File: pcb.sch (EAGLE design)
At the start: 57 parts, among them U2 ISO7221A_D_8, U3 MAX232E_D_16, U4 ISO7221A_D_8, U5 DCH010505S_EDJ_4, U6 REG101-3_DBV_5, U7 DCH010505S_EDJ_4, U8 MSP430G2553_PW_28

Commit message: Updated UART and expansion plug
Moved to true dual UART (one timer based)
Added remaining unused pins to expansion plug
finished first draft routing...no DRC check
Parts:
- removed U$4, U$5: TS5A3159-Q1, TI:TS5A3159-Q1
- JP10: device jumper:JP6Q -> jumper:JP8Q
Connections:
- removed net RX: U$4.COM, U8.P1.1/TA0.0/UCA0RXD/UCA0SOMI/A1/CA1
- removed net TX: U$5.COM, U8.P1.2/TA0.1/UCA0TXD/PUCA0SIMO/A2/CA2
- removed net UART_MODE: U$4.IN, U$5.IN, U8.P3.5/TA0.1
- new net GPIO1: JP10.11, U8.P3.7/TA1CLK/CAOUT
- new net GPIO2: JP10.13, U8.P3.6/TA0.2
- new net GPIO3: JP10.16, U8.P3.4/TA0.0
- net ENCODER_A_MCU: now also U8.P2.0/TA1.0; no longer U8.P1.5/TA0.0/UCB0CLK/UCA0STE/A5/CA5/TMS
- net ENCODER_B_MCU: now also C25.2, R8.2; no longer C26.1, R9.2
- net ENCODER_PUSH: now also C26.1, R9.2; no longer C25.2, R8.2
- net GND: now also JP10.3; no longer JP10.2, U$4.GND, U$5.GND
- net LASER_ON: now also JP10.14; no longer JP10.5
- net N$18: now also JP10.7; no longer JP10.9
- net N$19: now also JP10.5; no longer JP10.7
- net RST: now also JP10.15
- net RX1: now also U8.P1.1/TA0.0/UCA0RXD/UCA0SOMI/A1/CA1; no longer U$4.NC
- net RX2: now also U8.P1.5/TA0.0/UCB0CLK/UCA0STE/A5/CA5/TMS; no longer U$4.NO
- net SCL: now also JP10.9; no longer JP10.11
- net TX1: now also U8.P1.2/TA0.1/UCA0TXD/PUCA0SIMO/A2/CA2; no longer U$5.NC
- net TX2: now also U8.P3.5/TA0.1; no longer U$5.NO
- net VCC_3V: no longer U$4.VCC, U$5.VCC
- net VCC_5V: now also JP10.2; no longer JP10.3
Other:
- moved on the sheet: C1, C10, C11, C12, C13, C14, C15, C16, C17, C18, C19, C20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

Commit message: updated layout and board
Fixed interlock design
Added analog front end to analog inputs
changed MCU to MSP450 5 series
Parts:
- removed C22, C23, C24, C25, C26, C27: (no value), adafruit:C-USC1206
- removed JP10: (no value), jumper:JP8Q
- removed QF1: 10G7A-12.5KHZ, crystal:10G7A-12.5KHZ
- removed R12: (no value), adafruit:R-US_M1206
- removed U$3: TS5A3159-Q1, TI:TS5A3159-Q1
- added C2, C29: 2.2 uF, adafruit:C-USC1206
- added C30: 4.7 uF, adafruit:C-USC1206
- added C31, C32, C33, C34: 0.1 uF, adafruit:C-USC1206
- added JP2: (no value), adafruit:PINHD-2X4
- added JP3, JP6: (no value), jumper:JP2E
- added Q2: (no value), adafruit:XTAL-4-3225
- added R14: 500k, adafruit:R-US_M1206
- added R15: 10k, adafruit:R-US_M1206
- added R4: (no value), adafruit:R-US_M1206
- added SV1: (no value), con-lsta:FE08-2
- added SV3: (no value), con-lsta:FE06-2
- added U$4: 10k, adafruit:TRIMPOTTC33X
- added U$5: 100 nF, TI:468M-801-XXX
- added U$6: 3 uH, adafruit:FB
- added U1: MSP430F5172_DA_38, TI:MSP430F5172_DA_38
- added U10: DCH010505S_EDJ_4, TI:DCH010505S_EDJ_4
- added U11: ISO7221A_D_8, TI:ISO7221A_D_8
- added U12, U13: TS5A3357_DCU_8, TI:TS5A3357_DCU_8
- added U14: TLV2242_D_8, TI:TLV2242_D_8
- C1, C6, C7, C8: value (none) -> 1 uF
- C10, C11, C12, C18, C19, C3, C4: value (none) -> 0.1 uF
- C13, C16: value (none) -> 2.2 uF
- C14, C17: value (none) -> 4.7 uF
- C15, C5: value (none) -> 10 uF
- C20: value (none) -> 0.01 uF
- C9: value (none) -> 2.2 nF
- JP4: device jumper:JP4E -> con-lsta:FE07-2
- JP7: device con-subd:F09HP -> jumper:JP2E
- R1: value (none) -> 1M; device adafruit:R-US_M1206 -> adafruit:R-US_R1206
- R10: value (none) -> 47k
- R11: value (none) -> 750k
- R2, R3: value (none) -> 43k
- R5: value (none) -> 500k
- R6: value (none) -> 0R; device adafruit:R-US_M1206 -> adafruit:R-US_R1206
- R7: value (none) -> 100k; device adafruit:R-US_M1206 -> resistor-bourns:2QSP16-8
- R8: value (none) -> 600k; device adafruit:R-US_M1206 -> adafruit:R-US_R1206
- R9: value (none) -> 400k; device adafruit:R-US_M1206 -> adafruit:R-US_R1206
- U$1, U$2: value FB -> 3 uH
- U8: value MSP430G2553_PW_28 -> TCA6416A_PW_24; device TI:MSP430G2553_PW_28 -> TI:TCA6416A_PW_24
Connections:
- net N$20 renamed SERIAL_VCC
- removed net ENCODER_A_MCU: C27.1, R10.2, U8.P2.0/TA1.0
- removed net ENCODER_B_MCU: C25.2, R8.2, U8.P3.0/TA0.2
- removed net ENCODER_PUSH: C26.1, R9.2, U8.P3.1/TA1.0
- removed net GPIO1: JP10.11, U8.P3.7/TA1CLK/CAOUT
- removed net GPIO2: JP10.13, U8.P3.6/TA0.2
- removed net GPIO3: JP10.16, U8.P3.4/TA0.0
- removed net LASER_ENABLE: U8.P2.3/TA1.0, X2.1
- removed net LASER_ILK_LED: R11.2, U8.P2.2/TA1.1
- removed net LASER_ON: JP10.14, U8.P3.3/TA1.2
- removed net LASER_ON_LED: R12.2, U8.P3.2/TA1.1
- removed net MCU_TTL: U$3.NC, U2.INA, U8.P2.5/TA1.2
- removed net N$16: C22.1, QF1.3, R7.2
- removed net N$19: JP10.5, R12.1
- removed net TTL_CTL: U$3.IN, U8.P2.4/TA1.2
- new net 3VIO-0: R7.15, U1.PJ.0/SMCLK/TDO/CB6
- new net 3VIO-0H: R7.8, SV3.1, U$5.1
- new net 3VIO-1: R7.14, U1.PJ.1/MCLK/TDI/TCLK/CB7
- new net 3VIO-1H: R7.7, SV3.2, U$5.2
- new net 3VIO-2: R7.13, U1.PJ.2/ADC10CLK/TMS/CB8
- new net 3VIO-2H: R7.6, SV3.4, U$5.3
- new net 3VIO-3: R7.12, U1.PJ.3/ACLK/TCK/CB9
- new net 3VIO-3H: R7.5, SV3.6, U$5.4
- new net 3VIO-4: R7.11, U1.P3.3/PM_TA0CLK/PM_CBOUT/CB13
- new net 3VIO-4H: R7.4, SV3.8, U$5.5
- new net 3VIO-5: R7.10, U1.P3.2/PM_TD0.0/PM_SMCLK/CB14
- new net 3VIO-5H: R7.3, SV3.10, U$5.6
- new net 3VIO-6: R7.9, U1.PJ.6/TD1CLK/TD0.1/CB15
- new net 3VIO-6H: R7.2, SV3.12, U$5.7
- new net 5VIO-0: JP2.7, U1.P1.6/PM_TD0.0
- new net 5VIO-1: JP2.5, U1.P2.0/PM_TD0.2
- new net 5VIO-2: JP2.3, U1.P2.1/PM___TD1.0
- new net 5VIO-3: JP2.1, U1.P2.2/PM_TD1.1
- new net CONTRAST: SV1.3, U$4.S
- new net DB0: SV1.7, U8.P00
- new net DB1: SV1.8, U8.P01
- new net DB2: SV1.9, U8.P02
- new net DB3: SV1.10, U8.P03
- new net DB4: SV1.11, U8.P04
- new net DB5: SV1.12, U8.P05
- new net DB6: SV1.13, U8.P06
- new net DB7: SV1.14, U8.P07
- new net ENABLE: SV1.6, U8.P11
- new net EXT_SRC-A: U1.P2.5/PM_TEC0FLT0/PM_TD0.1, U13.IN1
- new net EXT_SRC-B: U1.P2.4/PM_TEC0CLR/PM_TEC0FLT2_/PM_TD0.0, U13.IN2
- new net EXT_TTL: JP2.2, U12.NO1, U13.NO1
- new net ITL_POWER: C29.1, U$6.2, U10.VI+
- new net LASER_CURRENT_3V: U1.P1.0/PM_UCA0CLK/PM_UCB0STE/A0*/CB0, U14.1IN-, U14.1OUT
- new net LASER_ILK_HIGH: R11.1, U11.OUTA
- new net LASER_SRC-A: U1.P2.7/PM_TEC1CLR/PM_TEC1FLT1/PM_TD1.0, U12.IN1
- new net LASER_SRC-B: U1.P2.6/PM_TEC0FLT1/PM_TD0.2, U12.IN2
- new net LASER_TEMPERATURE_3V: U1.P1.3/PM_UCB0CLK/PM_UCA0STE/A3*/CB3, U14.2IN-, U14.2OUT
- new net MCU_TTL1: U1.P3.1/PM_TEC1FLT0/PM_TD1.2, U12.NO0, U13.NO2
- new net MCU_TTL2: U1.P3.0/PM_TEC1FLT2/PM_TD1.1, U13.NO0
- new net N$21: Q2.X1, U1.PJ.4/XOUT
- new net N$22: Q2.X2, U1.PJ.5/XIN
- new net N$24: C34.1, U1.VCORE
- new net N$27: C2.1, R14.2, U10.VO+, U11.VCC2
- new net N$28: C2.2, JP3.3, U10.VO-, U11.GND2
- new net N$35: JP3.1, R14.1
- new net R/W: SV1.5, U8.P12
- new net RS: SV1.4, U8.P10
- new net TTL_OUT: U13.COM, U2.INA
- new net VCC_LED: R4.1, SV1.15
- net GND: now also C29.2, C30.2, C31.2, C32.2, C33.2, C34.2, JP2.6, JP4.9, Q2.G1, R1.1, R8.1, SV1.1, SV1.16, SV3.5, U$4.A, U$5.BUS, U$5.BUS2, U1.AVSS, U1.DVSS, U1.DVSS_2, U10.VI-, U11.GND1, U12.GND, U13.GND, U14.GND, U8.GND; no longer C22.2, C23.2, C24.2, C25.1, C26.2, C27.2, JP10.3, JP4.3, QF1.2, U$3.GND, U8.DVSS
- net LASER_CURRENT: now also R9.2; no longer U8.P1.0/TA0CLK/ACLK/A0/CA0
- net LASER_ILK: now also R11.2, U1.P2.3/PM_TD1.2, X2.1; no longer JP10.4, R1.1, U8.P2.1/TA1.1
- net LASER_TEMPERATURE: now also R6.2; no longer U8.P1.3/ADC10CLK/CAOUT/VREF-/VEREF-/A3/CA3
- net LASER_TTL: now also U12.COM; no longer U$3.COM
- net N$10: now also R8.2, R9.1, U14.1IN+; no longer JP10.8, R8.1
- net N$12: now also R5.2, U11.INA; no longer R5.1, U8.XIN/P2.6/TA0.1
- net N$14: now also JP3.2, R5.1; no longer R7.1, U8.XOUT/P2.7
- net N$15: now also R15.1, U8.*RESET; no longer C9.1, QF1.1, R5.2
- net N$17: now also JP4.2, JP7.3; no longer JP10.10, R10.1
- net N$18: now also JP4.4, JP7.1; no longer JP10.7, R11.1
- net N$8: now also R1.2, R6.1, U14.2IN+; no longer JP10.6, R9.1
- net RS232_RX: now also JP6.3; no longer JP7.2
- net RS232_TX: now also JP6.2; no longer JP7.3
- net RST: now also C9.1, JP4.1, R10.1, U1.*RST/NMI/SBWTDIO; no longer C24.1, JP10.15, JP4.2, R6.1, U8.*RST/NMI/SBWTDIO
- net RX1: now also U1.P1.2/PM_UCA0RXD/PM_UCA0SOMI/A2*/CB2; no longer U8.P1.1/TA0.0/UCA0RXD/UCA0SOMI/A1/CA1
- net RX2: now also U1.P3.6/PM_TA0.1/A7*/VEREF-*_/CB11; no longer U8.P1.5/TA0.0/UCB0CLK/UCA0STE/A5/CA5/TMS
- net SCL: now also SV3.7, U1.P1.5/PM_UCB0SOMI/PM_UCB0SCL/A5*/CB5, U8.SCL; no longer JP10.9, U8.P1.6/TA0.1/UCB0SOMI/UCB0SCL/A6/CA6/TDI/TCLK
- net SDA: now also SV3.9, U1.P1.4/PM_UCB0SIMO/PM_UCB0SDA/A4*/CB4, U8.SDA; no longer JP10.12, U8.P1.7/CAOUT/UCB0SIMO/UCB0SDA/A7/CA7/TDO/TDI
- net SERIAL_GND: now also JP6.1; no longer JP7.5, JP7.G1, JP7.G2
- net TEST: now also JP4.7, U1.TEST/SBWTCK; no longer JP4.1, U8.TEST/SBWTCK
- net TTL_IN: now also JP2.4, U1.P1.7/PM_TD0.1, U12.NO2; no longer U$3.NO, U8.P1.4/SMCLK/UCB0STE/UCA0CLK/VREF+/VEREF+/A4/CA4/TCK
- net TX1: now also U1.P1.1/PM_UCA0TXD/PM_UCA0SIMO/A1*/CB1; no longer U8.P1.2/TA0.1/UCA0TXD/PUCA0SIMO/A2/CA2
- net TX2: now also U1.P3.5/PM_TA0.2/A8*/VEREF+*/CB12; no longer U8.P3.5/TA0.1
- net VCC_3V: now also C31.1, C32.1, JP7.2, R10.2, R15.2, SV3.3, U1.AVCC, U1.DVCC, U14.VCC, U8.VCCI; no longer C23.1, C3.2, JP10.1, JP4.4, R1.2, R6.2, U$3.VCC, U2.VCC2, U8.DVCC
- net VCC_5V: now also C3.2, C30.1, C33.1, JP2.8, R4.2, SV1.2, U$4.E, U$6.1, U1.DVIO, U11.VCC1, U12.V+, U13.V+, U2.VCC2, U8.ADDR, U8.VCCP; no longer JP10.2
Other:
- note added: "100 nF"
- note added: "Analog input buffers -------------------------------------------------- Laser outputs two analog channels relating diode current and temperature. Buffering stage provides level conversion and protection to the MCU"
- note added: "Front Panel Header -------------------------------------------------- Provides 8 filtered 3V GPIO lines plus data and power for front panel buttons and indicator lights"
- note added: "I2C Pull up ----------------------------"
- note added: "JTAG ICSP -------------------------------------------------- 2W (SBW) JTAG programming header Local Power: bridge JP7 1 & 2 Programmer Power: bridge JP7 2 & 3"
- note added: "LCD interface ------------------------------------------------- LCD is interfaced through I2C port expander"
- note added: "Laser Connector ---------------------------------------- DB25 connector sourcing power and data to laser. Must source/sink 10A @5V"
- note added: "Laser Interlock ------------------------------ Enabled when pins 1 and 2 on JP3 are shorted. Interlock is monitored by MCU and can be disabled by pulling the line low"
- note added: "Laser SRC Truth table (U12) ------------------------------------ A B Function 0 0 All off 1 0 MCU Timer output 0 1 Expansion Port output 1 1 External Reference External SRC Truth table (U13) ------------------------------------ A B Function 0 0 All off 1 0 MCU Timer 2 output 0 1 Expansion Port output 1 1 MCU Timer 1 output"
- note added: "Laser Triggering --------------------------------------------------- Laser can be triggered from: 1. Internal MCU generated trigger 2. External trigger 3. Trigger generated by expansion card (hardware delay)"
- note added: "Microcontroller ---------------------------------------------- MSP430F5172 Microcontroller provides monitoring and control over laser. Interfaces include front panel and dual UARTS. Microncontroller has both 3V and 5V IO (5V in bold). 5V IO reserved for digital IO with laser and hardware delay expansion card 3V IO is used for front panel controls. MCU uses TimerD facility to generate dual PWM out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"
- note added: "Power ----------------------------------------------------- Input power: 5V Regulated to 3V for digital circuit MCU runs both 3 and 5V IO"
- note added: "Serial Communication ------------------------------------------------------ JP6: Isolated RS232 with translation to (hardware) 3V UART JP1: Header for UART to BT serial adaptor. (requires timer serial)"
- moved on the sheet: C1, C10, C11, C12, C13, C14, C15, C16, C17, C18, C19, C20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

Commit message: Silk Screen and analog front end
Update to documentation on silk screen
Addition of buffered voltage divider for analog front end
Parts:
- U1: value MSP430F5172_DA_38 -> MSP430F5172
- U11: value ISO7221A_D_8 -> ISO7420_D_8; device TI:ISO7221A_D_8 -> TI:ISO7420_D_8; DATASHEETURL (none) -> http://www.ti.com/lit/gpn/ISO7420; DESCRIPTION (none) -> Low Power Dual Channel Isolators; GENERIC_PART_NUMBER (none) -> ISO7420; MANUFACTURER_PART_NUMBER (none) -> iso7420_d_8
- renumbered U$1 to I2, U$2 to I3, U$4 to VR1, U$6 to I1
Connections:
- removed net N$12: R5.2, U11.INA
- new net N$19: R5.2, U11.INA, U11.INB
- net GND: now also SV3.11, U11.VCC2; no longer U11.GND1
- net LASER_ILK_HIGH: now also U11.OUTB
- net N$27: now also U11.VCC1; no longer U11.VCC2
- net N$28: now also U11.GND1; no longer U11.GND2
- net VCC_5V: now also U11.GND2; no longer U11.VCC1
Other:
- moved on the sheet: U11

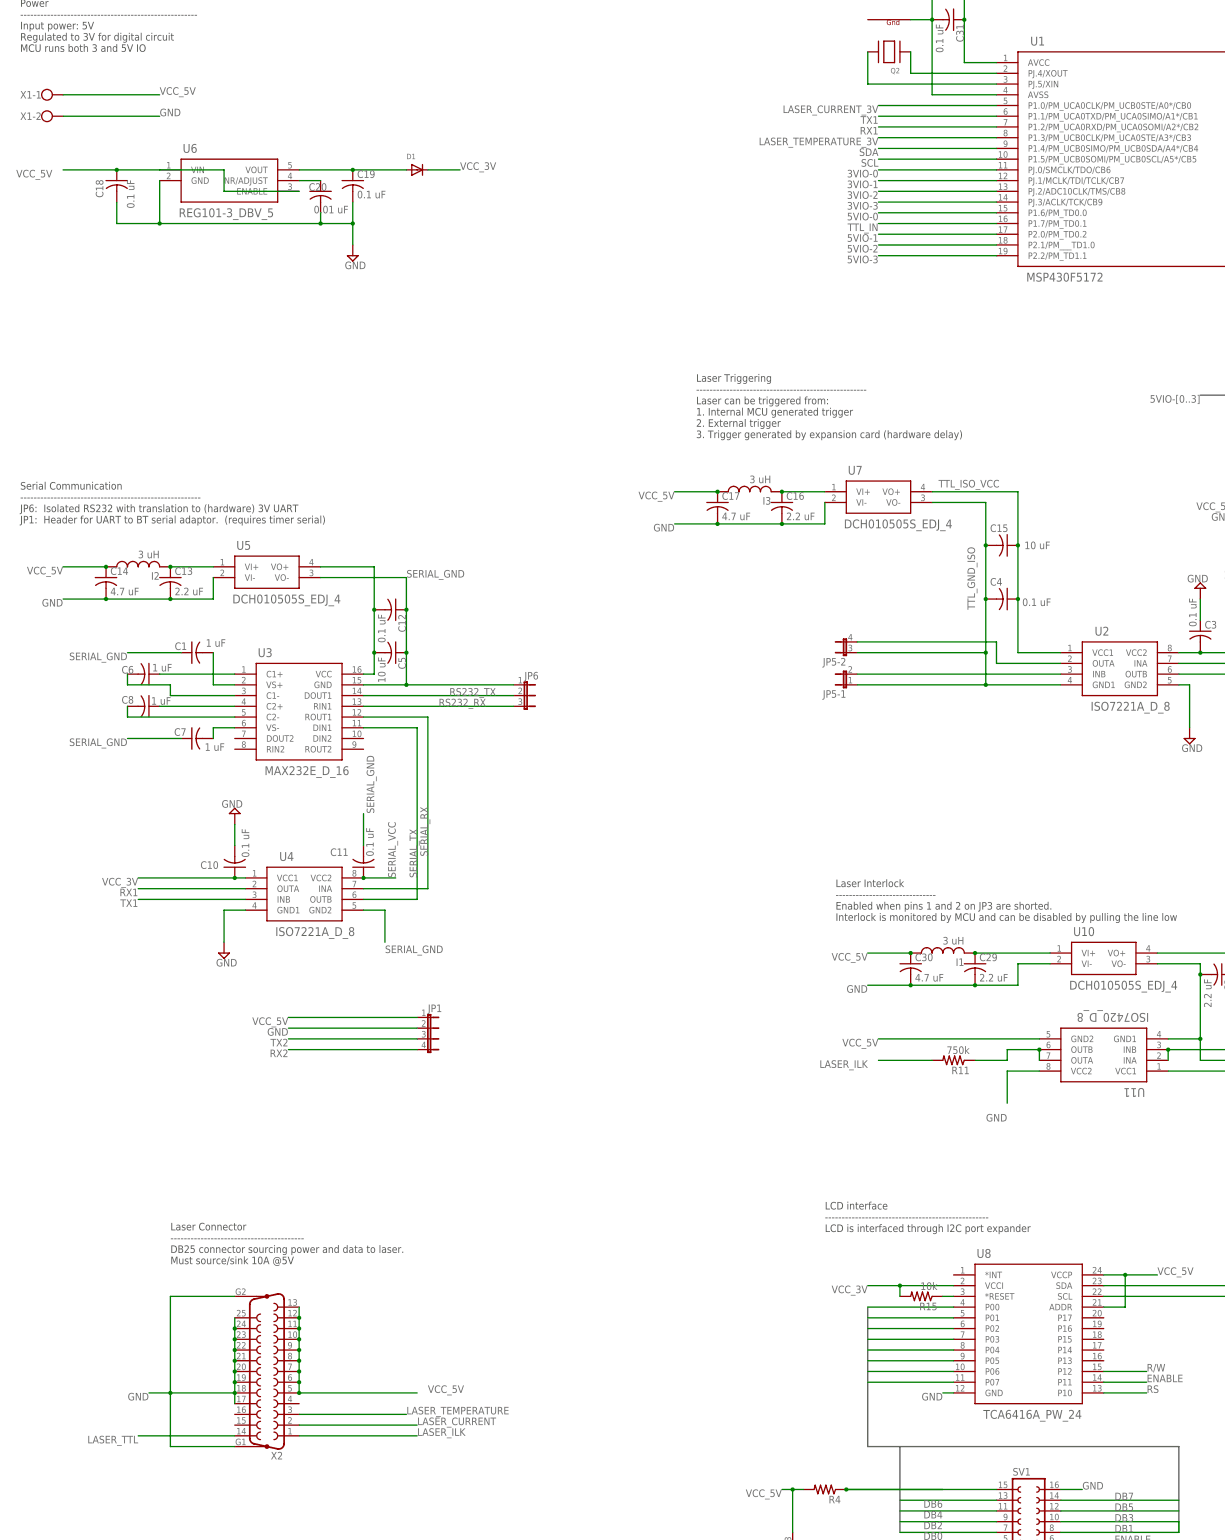
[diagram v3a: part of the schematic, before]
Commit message: Extensive Silkscreen update, LEDS
Added power, rx and tx LEDs
Updates silk screen documentation
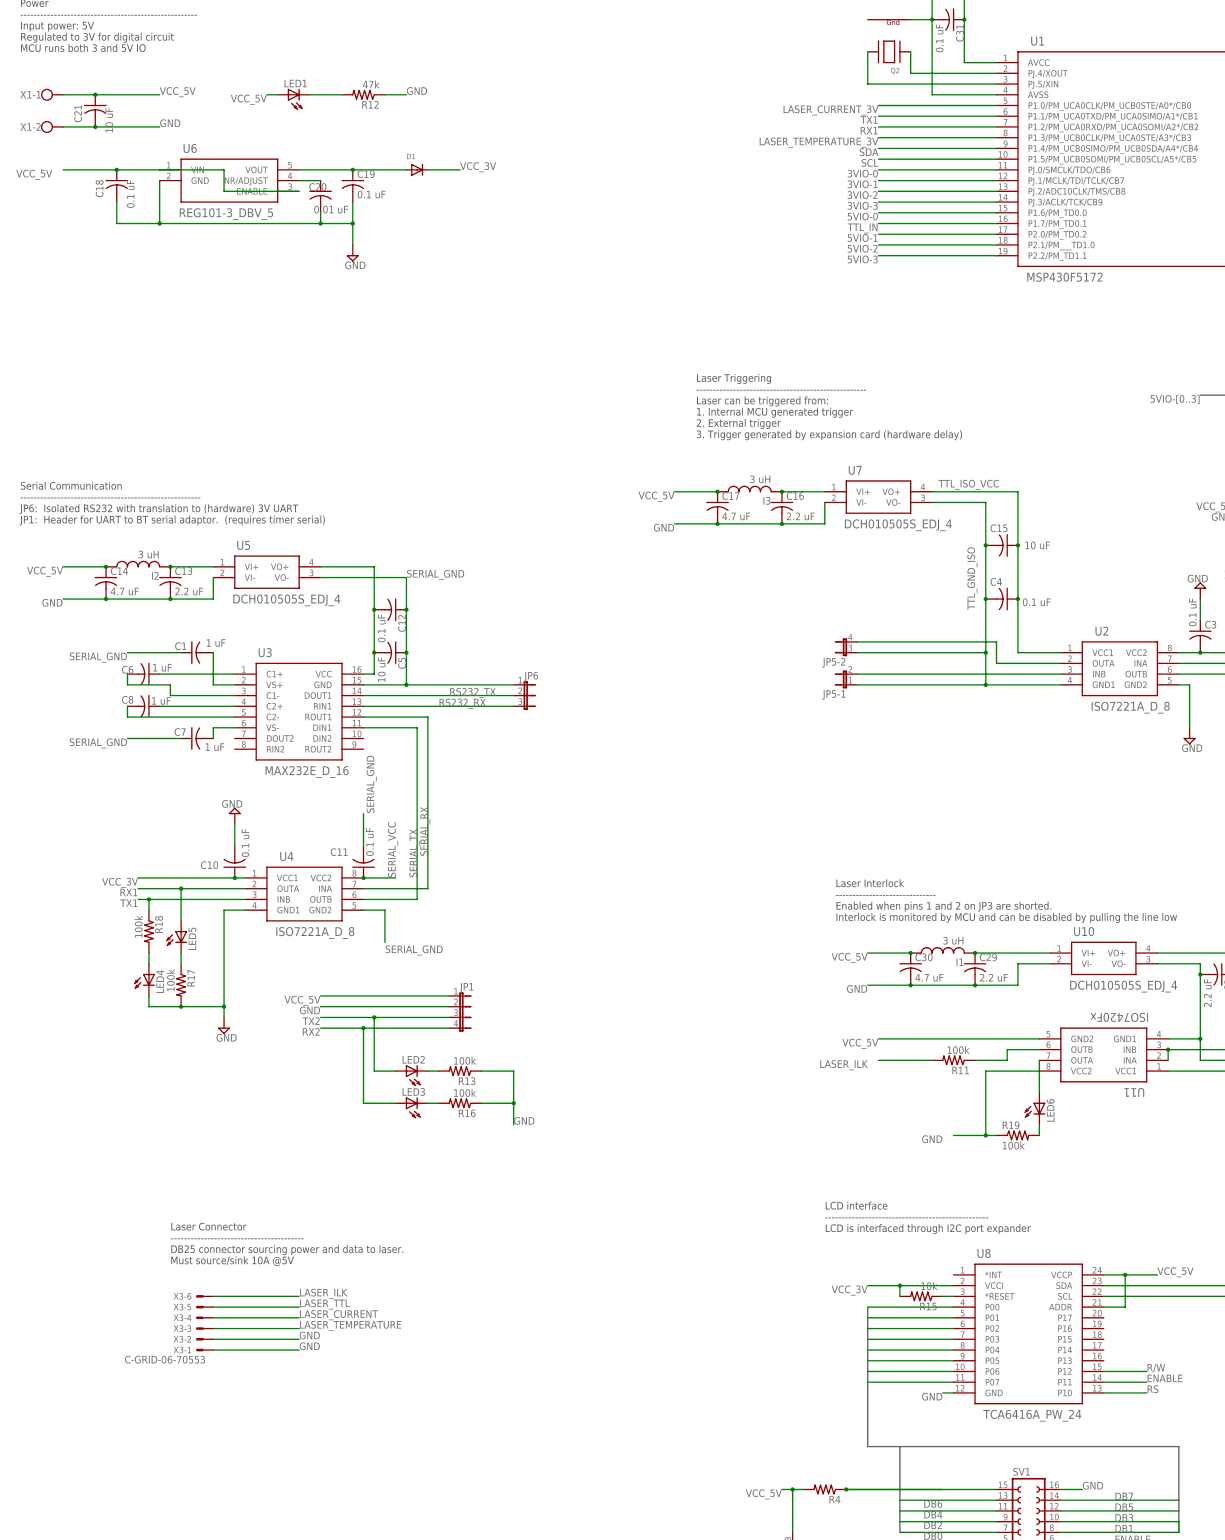
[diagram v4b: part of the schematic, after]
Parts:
- removed X2: (no value), con-subd:F25VP
- added C21: 10 uF, adafruit:C-USC1206
- added LED1, LED2, LED3, LED4, LED5, LED6: (no value), led:LEDSMT1206
- added R12: 47k, adafruit:R-US_M1206
- added R13, R16, R17, R18, R19: 100k, adafruit:R-US_M1206
- added X3: C-GRID-06-70553, con-molex:C-GRID-06-70553
- R11: value 750k -> 100k
- U11: value ISO7420_D_8 -> ISO7420Fx
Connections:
- new net N$25: LED1.C, R12.2
- new net N$26: LED2.C, R13.2
- new net N$29: LED3.C, R16.2
- new net N$30: LED6.C, R19.2
- new net N$31: LED5.C, R17.1
- new net N$32: LED6.A, U11.OUTA
- new net N$33: LED4.A, R18.2
- net GND: now also C21.2, LED4.C, R12.1, R13.1, R16.1, R17.2, R19.1, X3-1.S, X3-2.S; no longer X2.17, X2.18, X2.19, X2.20, X2.21, X2.22, X2.23, X2.24, X2.25, X2.G1, X2.G2
- net LASER_CURRENT: now also X3-4.S; no longer X2.2
- net LASER_ILK: now also X3-6.S; no longer X2.1
- net LASER_ILK_HIGH: no longer U11.OUTA
- net LASER_TEMPERATURE: now also X3-3.S; no longer X2.3
- net LASER_TTL: now also X3-5.S; no longer X2.14
- net RX1: now also LED5.A
- net RX2: now also LED3.A
- net TX1: now also R18.1
- net TX2: now also LED2.A
- net VCC_5V: now also C21.1, LED1.A; no longer X2.10, X2.11, X2.12, X2.13, X2.5, X2.6, X2.7, X2.8, X2.9
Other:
- moved on the sheet: JP1, X1-2

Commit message: Silk updates
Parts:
- renumbered C1 to C8.5, C10 to C8.10, C11 to C8.9, C12 to C8.3, C13 to C8.2, C14 to C8.1, C15 to C6.3, C16 to C6.2, C17 to C6.1, C18 to C1.2, C19 to C1.4, C2 to C9.3, C20 to C1.3, C21 to C1.1, C29 to C9.2, C3 to C6.5, C30 to C9.1, C31 to C5.1, C32 to C5.2, C33 to C5.4, C34 to C5.3, C4 to C6.4, C5 to C8.4, C6 to C8.6, C7 to C8.8, C8 to C8.7, C9 to C7.1, I1 to L9.1, I2 to L8.1, I3 to L6.1, JP1 to H8.2, JP2 to H6.1, JP3 to H9.1, JP5 to H6.2, JP6 to H8.1, JP7 to H7.1, LED2 to LED8.3, LED3 to LED8.4, LED4 to LED8.1, LED5 to LED8.2, LED6 to LED9.1, Q2 to XTL, R1 to R4.1, R10 to R7.1, R11 to R9.1, R12 to R1.1, R13 to R8.3, R14 to R9.2, R15 to R2.1, R16 to R8.4, R17 to R8.2, R18 to R8.1, R19 to R9.4, R2 to R5.1, R3 to R5.2, R4 to R2.2, R5 to R9.3, R6 to R4.2, R7 to R3.1, R8 to R4.3, R9 to R4.4, SV1 to H2.1, SV3 to H3.1, U$5 to C3.1, U1 to MCU, U10 to U9.1, U11 to U9.2, U12 to U6.3, U13 to U6.4, U14 to U4.1, U2 to U6.2, U3 to U8.2, U4 to U8.3, U5 to U8.1, U6 to U1.1, U7 to U6.1, U8 to U2.1, X1 to EXT_POWER, X3 to LASER_COM
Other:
- note added: "Laser SRC Truth table (U6.3) ------------------------------------ A B Function 0 0 All off 1 0 MCU Timer output 0 1 Expansion Port output 1 1 External Reference External SRC Truth table (U6.4) ------------------------------------ A B Function 0 0 All off 1 0 MCU Timer 2 output 0 1 Expansion Port output 1 1 MCU Timer 1 output"
- note removed: "Laser SRC Truth table (U12) ------------------------------------ A B Function 0 0 All off 1 0 MCU Timer output 0 1 Expansion Port output 1 1 External Reference External SRC Truth table (U13) ------------------------------------ A B Function 0 0 All off 1 0 MCU Timer 2 output 0 1 Expansion Port output 1 1 MCU Timer 1 output"
